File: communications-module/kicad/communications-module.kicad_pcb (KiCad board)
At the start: 2 copper layers, 125.8 x 128.6 mm, 73 parts, among them J1 IDC12, P2 USB_A, P3 USB_A, P4 USB_A, P5 BACKUP, U1 nRF52832, U10 LIS3DH_breakout, U11 FONA_3G, U12 TPS2064, U13 RockBLOCK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

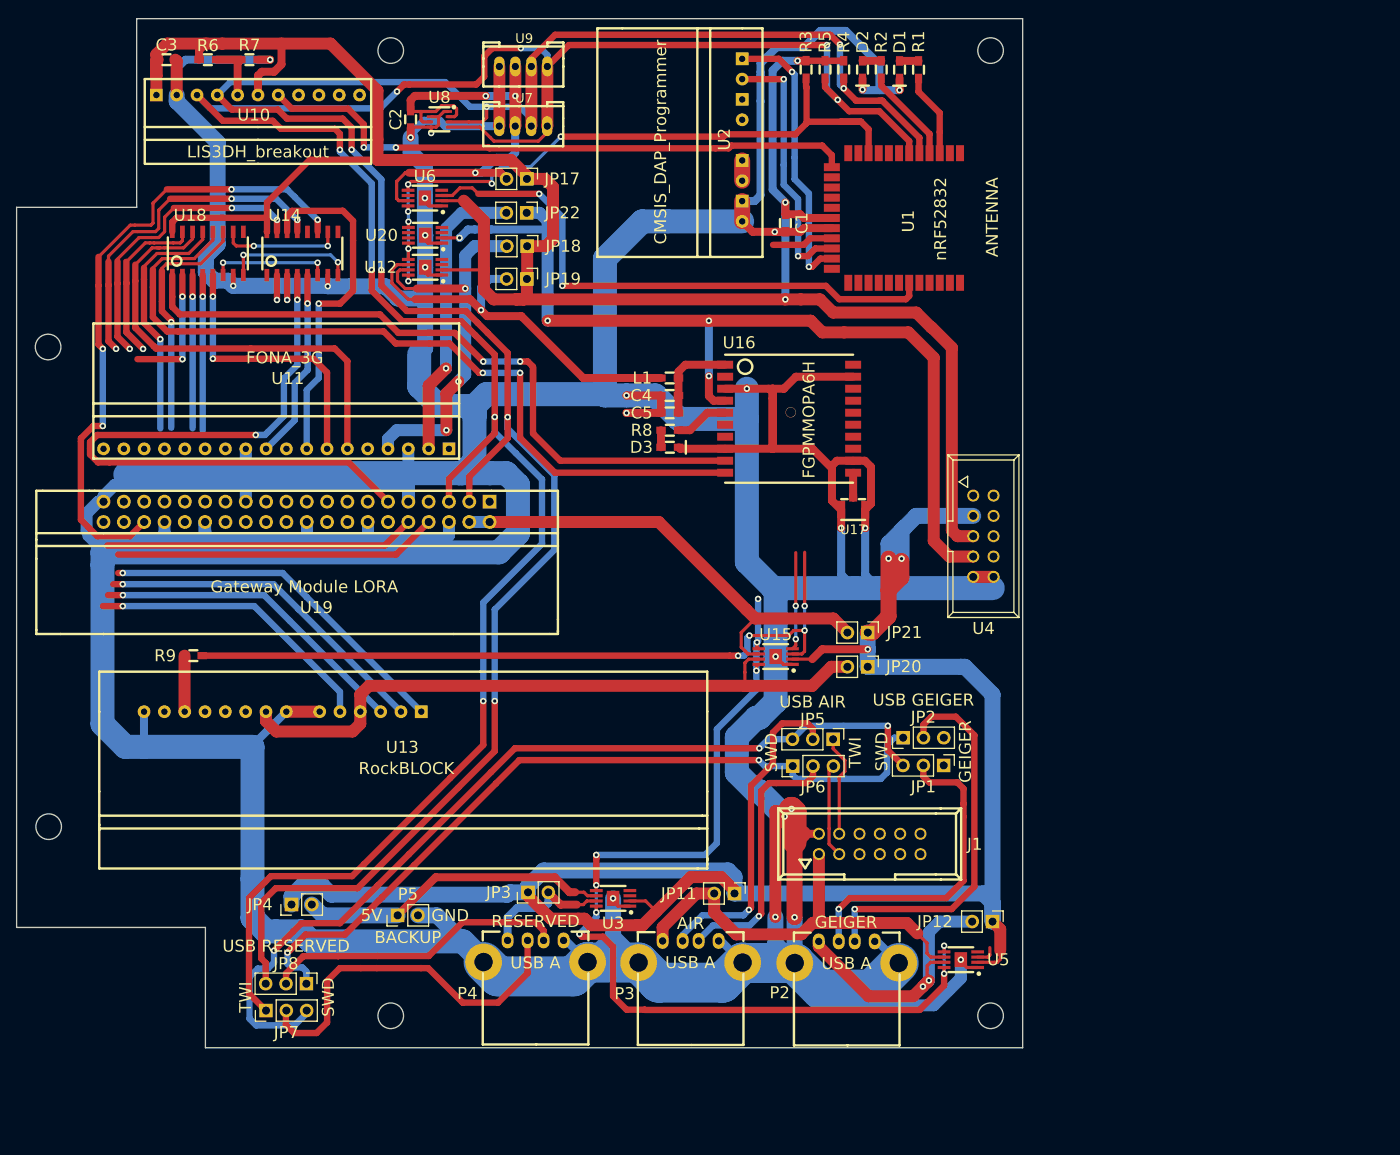
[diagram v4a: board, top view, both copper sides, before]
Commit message: Communications Module PCB update
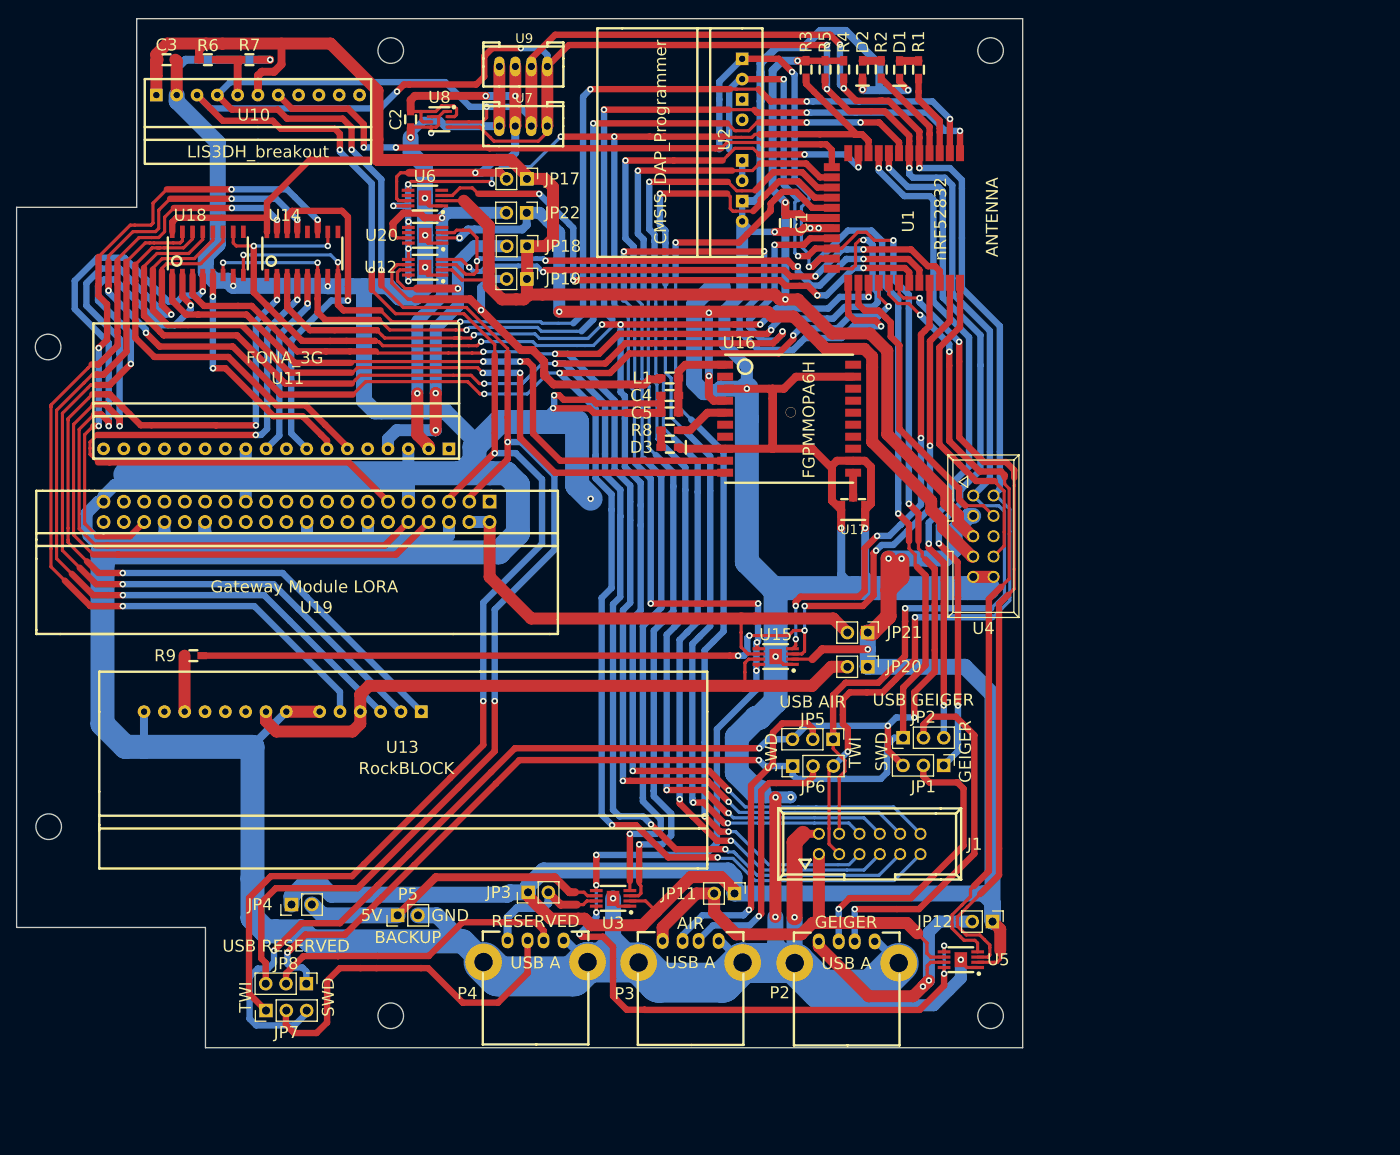
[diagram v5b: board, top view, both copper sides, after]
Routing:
- net UART_CTS: track 42.7 -> 251.0 mm, vias 3 -> 10
- net UART_TX: track 38.5 -> 229.2 mm, vias 1 -> 6
- net UART_RX: track 19.2 -> 206.0 mm, vias 1 -> 6
- net UART_RTS: track 3.10 -> 180.0 mm, vias 1 -> 7
- net ENABLE-BACKUP: track 0.00 -> 144.6 mm, vias 0 -> 4
- net SPI_MOSI: track 0.00 -> 135.5 mm, vias 0 -> 3
- net SPI_MISO: track 0.00 -> 135.4 mm, vias 0 -> 3
- net ENABLE-RESERV: track 0.00 -> 133.5 mm, vias 0 -> 4
- net UMUX_SEL0: track 15.1 -> 145.9 mm, vias 2 -> 6
- net SPI_CS: track 0.00 -> 128.0 mm, vias 0 -> 3
- net SPI_SCLK: track 0.00 -> 121.1 mm, vias 0 -> 3
- net UMUX_SEL1: track 16.3 -> 131.4 mm, vias 2 -> 6
- net UMUX_INH: track 14.9 -> 123.0 mm, vias 2 -> 6
- net TWI_SDA: track 305.3 -> 406.1 mm, vias 7 -> 10
- net ENABLE-GEIG: track 2.56 -> 100.0 mm, vias 0 -> 2
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
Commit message: Communications Module PCB update
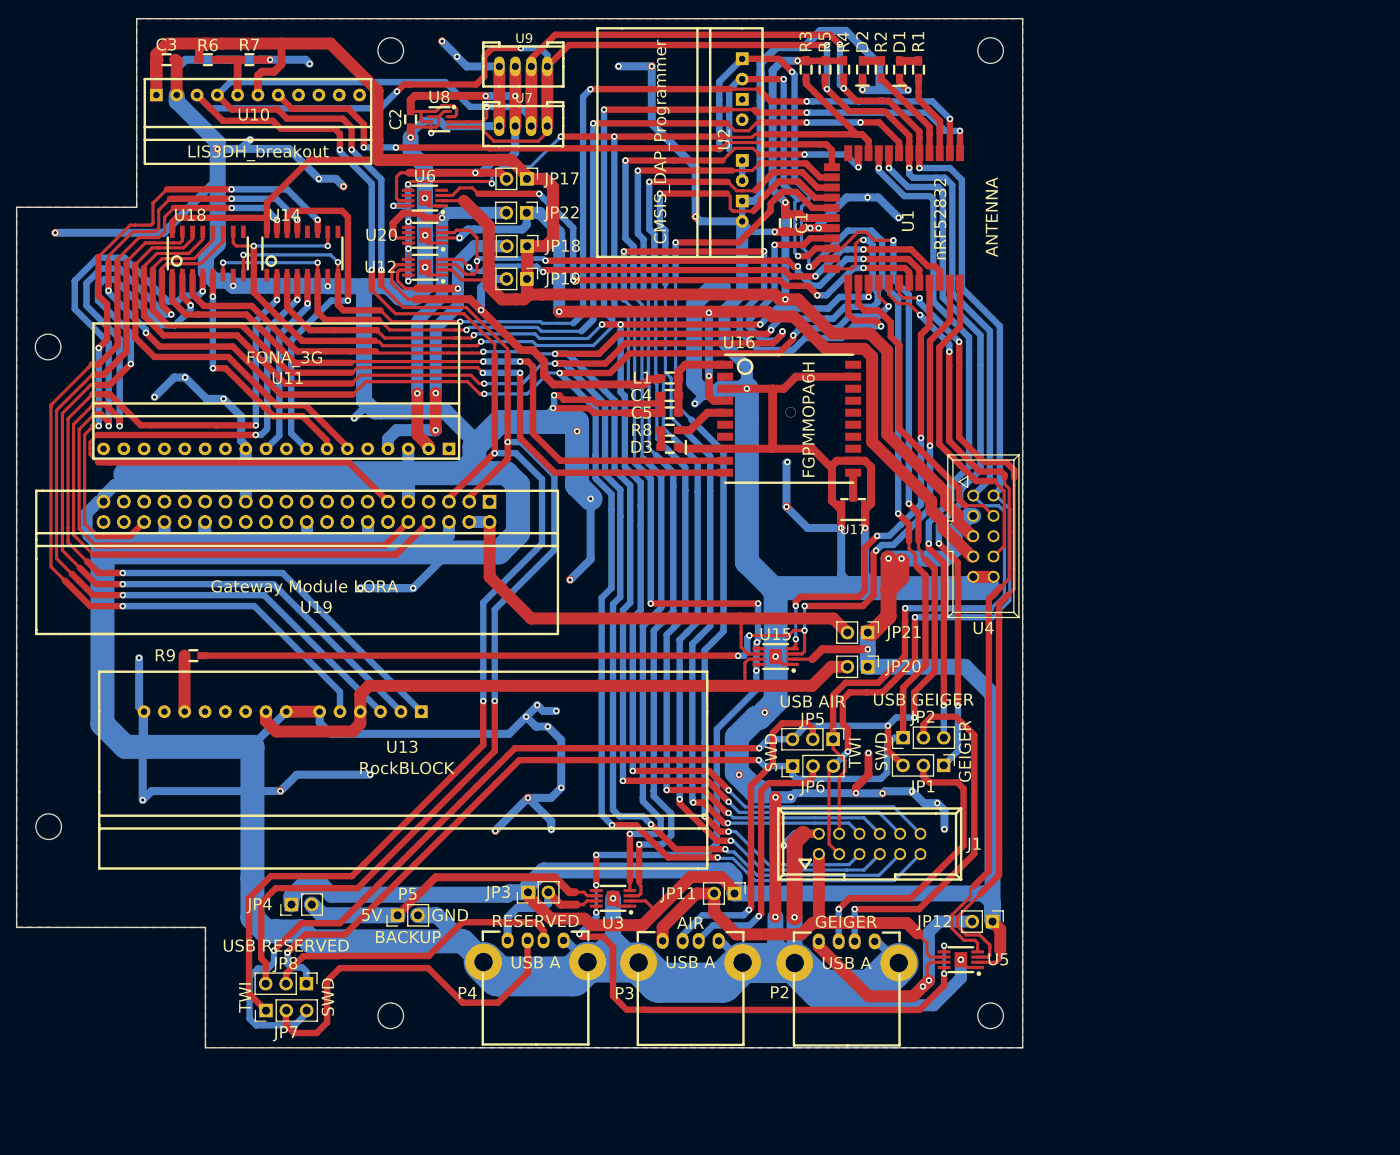
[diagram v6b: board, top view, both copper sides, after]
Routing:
- net GND: track 1019.5 -> 1349.3 mm, vias 27 -> 72
- added copper zone on B.Cu, net GND
- added copper zone on F.Cu, net GND
